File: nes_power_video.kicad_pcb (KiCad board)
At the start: 2 copper layers, 59.9 x 59.7 mm, 25 parts, among them J2 Audio, J3 Video, J4 Conn_01x05, J5 RGB conn feed, Q1 2SA733, U1 TPS2553DBV

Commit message: feat(power): add C4, a local 100nF bypass at the eFuse output
TI's TPS2553 layout guidelines (SLVSBM8, 12.1) ask for "a high-value
electrolytic capacitor and a 100-nF bypass capacitor on the output pin
when large transient currents are expected". /5V had neither locally.
C3 (100nF) bypasses the eFuse *input*; C1 (100uF) is the only thing on
the output and sits ~52mm of copper away, reached by a 20.5mm 0.2mm
spur that lands on D1's cathode pad. That routing is a fossil: C1
predates the eFuse (it was already placed when c00c4e2 inserted U1
into the middle of the rail), so the bulk cap ended up last in the
chain instead of at the source.

C4 is the same part as C3 (CC0805KRX7R9BB104, LCSC C49678) so this
adds a quantity, not a line, to the assembly BOM. Placed rotated 90
degrees at (32.3,35.5) so pad 1 lands directly on the /5V trace
leaving U1 pin 6 -- 3.56mm from the pin, against C1's 52mm -- with
pad 2 stitched to the B.Cu ground pour through its own via. The
rotation is what makes it fit: horizontal, the courtyard collided
with both R3 and R4. R6's reference text moved 2.6mm to clear C4's
pad 1.

This is an improvement, not a defect fix. Section 10.2.1.2.4 is
explicit that output capacitance "improves the performance of the
device" -- it is not a stability requirement, and the only stability
constraint in the datasheet (15k <= RILIM <= 232k) is already met by
R6 at 22k. Fabbed v2 boards are fine without it.

Verified: ERC 0 violations; DRC --schematic-parity --refill-zones
0 errors, 0 unconnected, 0 parity issues, and the warning count is
unchanged from before this commit (the same 6 pre-existing silkscreen
warnings on J2/J3); tools/check_nets.py passes with all 14 nets
identical between schematic and PCB.

Co-Authored-By: Claude Opus 5 <noreply@anthropic.com>
Claude-Session: https://claude.ai/code/session_01TQL5dscMjqktyVUuQL7XXJ
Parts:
- added C4: 100nF, Capacitor_SMD:C_0805_2012Metric_Pad1.18x1.45mm_HandSolder, F.Cu at (32.3, 35.5)
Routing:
- net GND: track 15.4 -> 16.9 mm, vias 7 -> 8
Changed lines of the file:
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@@
 		)
 	)
+	(footprint "Capacitor_SMD:C_0805_2012Metric_Pad1.18x1.45mm_HandSolder"
+		(layer "F.Cu")
+		(at 32.3 35.5 90)
+		(descr "Capacitor SMD 0805 (2012 Metric), square (rectangular) end terminal, IPC-7351 nominal with elongated pad for handsoldering. (Body size source: IPC-SM-782 page 76, https://www.pcb-3d.com/wordpress/wp-content/uploads/ipc-sm-782a_amendment_1_and_2.pdf, https://docs.google.com/spreadsheets/d/1BsfQQcO9C6DZCsRaXUlFlo91Tg2WpOkGARC1WS5S8t0/edit?usp=sharing)")
+		(tags "capacitor handsolder")
+		(property "Reference" "C4"
+			(at 4 0 90)
+			(layer "F.SilkS")
+			(effects
+				(font
+					(size 1 1)
+					(thickness 0.15)
+				)
+			)
+		)
+		(property "Value" "100nF"
+			(at 0 1.68 0)
+			(hide yes)
+			(layer "F.SilkS")
+			(effects
+				(font
+					(size 0.8 0.8)
+					(thickness 0.12)
+				)
+			)
+		)
+		(property "Datasheet" "https://www.lcsc.com/datasheet/C49678.pdf"
+			(at 0 0 0)
+			(layer "F.Fab")
+			(hide yes)
+			(effects
+				(font
+					(size 1.27 1.27)
+				)
+			)
+		)
+		(property "Description" "Unpolarized capacitor"
+			(at 0 0 0)
+			(layer "F.Fab")
+			(hide yes)
+			(effects
+				(font
+					(size 1.27 1.27)
+				)
+			)
+		)
+		(property "KiLib_Generator" "SMD_2terminal_chip_molded"
+			(at 0 0 0)
+			(layer "F.SilkS")
+			(hide yes)
+			(effects
+				(font
+					(size 1 1)
+					(thickness 0.15)
+				)
+			)
+		)
+		(property "Manufacturer" "YAGEO"
+			(at 0 0 0)
+			(layer "F.Fab")
+			(hide yes)
+			(effects
+				(font
+					(size 1.27 1.27)
+					(thickness 0.15)
+				)
+			)
+		)
+		(property "MPN" "CC0805KRX7R9BB104"
+			(at 0 0 0)
+			(layer "F.Fab")
+			(hide yes)
+			(effects
+				(font
+					(size 1.27 1.27)
+					(thickness 0.15)
+				)
+			)
+		)
+		(property "LCSC" "C49678"
+			(at 0 0 0)
+			(layer "F.Fab")
+			(hide yes)
+			(effects
+				(font
+					(size 1.27 1.27)
+					(thickness 0.15)
+				)
+			)
+		)
+		(property "Supplier Link" "https://www.lcsc.com/product-detail/C49678.html"
+			(at 0 0 0)
+			(layer "F.Fab")
+			(hide yes)
+			(effects
+				(font
+					(size 1.27 1.27)
+					(thickness 0.15)
+				)
+			)
+		)
+		(property "Spec" "100 nF +/-10%, 50 V, X7R, 0805 (any equivalent >=16 V X7R)"
+			(at 0 0 0)
+			(layer "F.Fab")
+			(hide yes)
+			(effects
+				(font
+					(size 1.27 1.27)
+					(thickness 0.15)
+				)
+			)
+		)
+		(attr smd)
+		(duplicate_pad_numbers_are_jumpers no)
+		(fp_line
+			(start -0.261252 -0.735)
+			(end 0.261252 -0.735)
+			(stroke
+				(width 0.12)
+				(type solid)
+			)
+			(layer "F.SilkS")
+		)
+		(fp_line
+			(start -0.261252 0.735)
+			(end 0.261252 0.735)
+			(stroke
+				(width 0.12)
+				(type solid)
+			)
+			(layer "F.SilkS")
+		)
+		(fp_rect
+			(start -1.88 -0.98)
+			(end 1.88 0.98)
+			(stroke
+				(width 0.05)
+				(type solid)
+			)
+			(fill no)
+			(layer "F.CrtYd")
+		)
+		(fp_rect
+			(start -1 -0.625)
+			(end 1 0.625)
+			(stroke
+				(width 0.1)
+				(type solid)
+			)
+			(fill no)
+			(layer "F.Fab")
+		)
+		(fp_text user "${REFERENCE}"
+			(at 0 0 0)
+			(layer "F.Fab")
+			(effects
+				(font
+					(size 0.5 0.5)
+					(thickness 0.08)
+				)
+			)
+		)
+		(pad "1" smd roundrect
+			(at -1.0375 0 90)
+			(size 1.175 1.45)
+			(layers "F.Cu" "F.Mask" "F.Paste")
+			(roundrect_rratio 0.212766)
+			(net "/5V")
+		)
+		(pad "2" smd roundrect
+			(at 1.0375 0 90)
+			(size 1.175 1.45)
+			(layers "F.Cu" "F.Mask" "F.Paste")
+			(roundrect_rratio 0.212766)
+			(net "GND")
+		)
+		(embedded_fonts no)
+		(model "${KICAD10_3DMODEL_DIR}/Capacitor_SMD.3dshapes/C_0805_2012Metric.step"
+			(offset
+				(xyz 0 0 0)
+			)
+			(scale
+				(xyz 1 1 1)
+			)
+			(rotate
+				(xyz 0 0 0)
+			)
+		)
+	)
 	(footprint "nes1:PJRAN1X1U03X"
 		(layer "F.Cu")
@@
 		(tags "resistor handsolder")
 		(property "Reference" "R6"
-			(at 0 -1.65 0)
+			(at 2.6 -1.65 0)
 			(layer "F.SilkS")
 			(effects
@@
 		(net "Net-(Q1-B)")
 	)
+	(segment
+		(start 32.3 34.4625)
+		(end 32.3 33.0)
+		(width 0.4)
+		(layer "F.Cu")
+		(net "GND")
+	)
+	(via
+		(at 32.3 33.0)
+		(size 0.6)
+		(drill 0.3)
+		(layers "F.Cu" "B.Cu")
+		(net "GND")
+	)
 	(zone

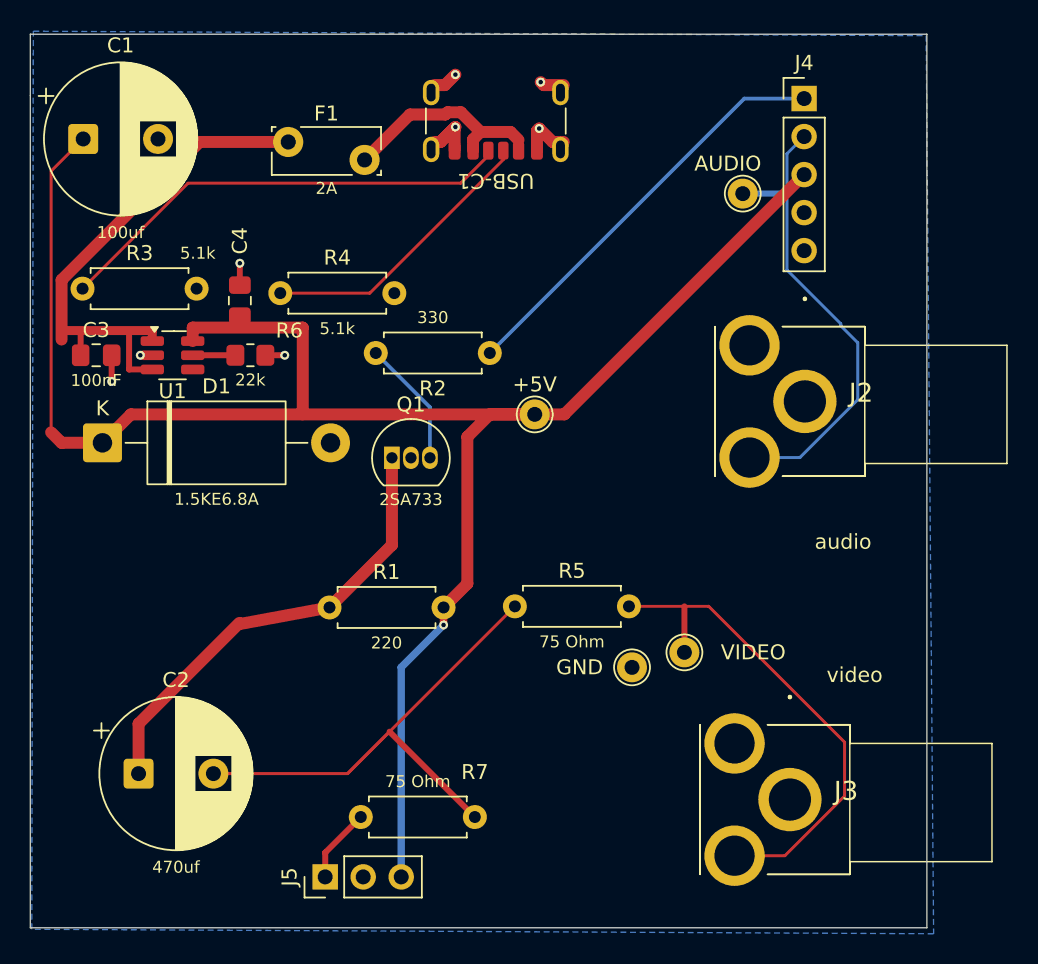
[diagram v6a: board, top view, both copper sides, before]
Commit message: fix(pcb): remove every overlapping track, and anchor C4's /5V connection
A geometric sweep for collinear same-net overlap found five pairs, not
the one spotted by eye in 2987996. Same-net overlap is invisible to
DRC, so none of these were ever reported.

  /5V         3.00mm  b7a635ae sat entirely inside the y=43.1 trunk
  /VIDEO_BUF  3.96mm  0d07e40b sat entirely inside a94ae6b3
  GND         1.27mm  4d3f7556 spanned what 387e46eb + 67cc2dcf already
  GND         0.14mm  the tail of that same knot
  /fused_5v   0.60mm  da31efaa doubled back over 1f43262f

The GND knot is resolved by deleting the single full-span segment
rather than the two-piece chain: 56acf260 lands on the intermediate
point (46.6,24.0), so keeping the chain preserves endpoint-to-endpoint
connectivity instead of relying on a T-junction.

/fused_5v needed a trim, not just a delete. 1f43262f overshot the
junction at (20.39,37.5) down to 38.1 and da31efaa doubled back up, so
removing the stub alone would have left a 0.6mm dangling tail. Its end
is now the junction itself.

Also anchors C4. Its pad 1 was touching the /5V trace only through a
1.45 x 0.225mm area overlap -- enough for KiCad to call it connected,
but far too little to rely on. An explicit 0.76mm stub from the pad
centre to the trace centreline now carries it.

Copper removed, per net, matching prediction exactly and touching
nothing else: /5V -3.000mm, /VIDEO_BUF -3.960mm, /fused_5v -1.200mm,
GND -1.414mm. Ten other nets unchanged to the picometre.

Verified: geometric overlap sweep 0 pairs across 92 segments; DRC
--schematic-parity --refill-zones 0 errors, 0 unconnected, 0 parity,
warnings unchanged at the 6 pre-existing J2/J3 silkscreen ones;
check_nets.py all invariants, 14/14 nets identical; and an independent
union-find over pads, tracks and vias confirms all 13 non-GND nets are
a single copper island each, with 0 of 63 pads outside the board
outline, 0 pads lacking track contact and 0 dangling endpoints.

Co-Authored-By: Claude Opu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
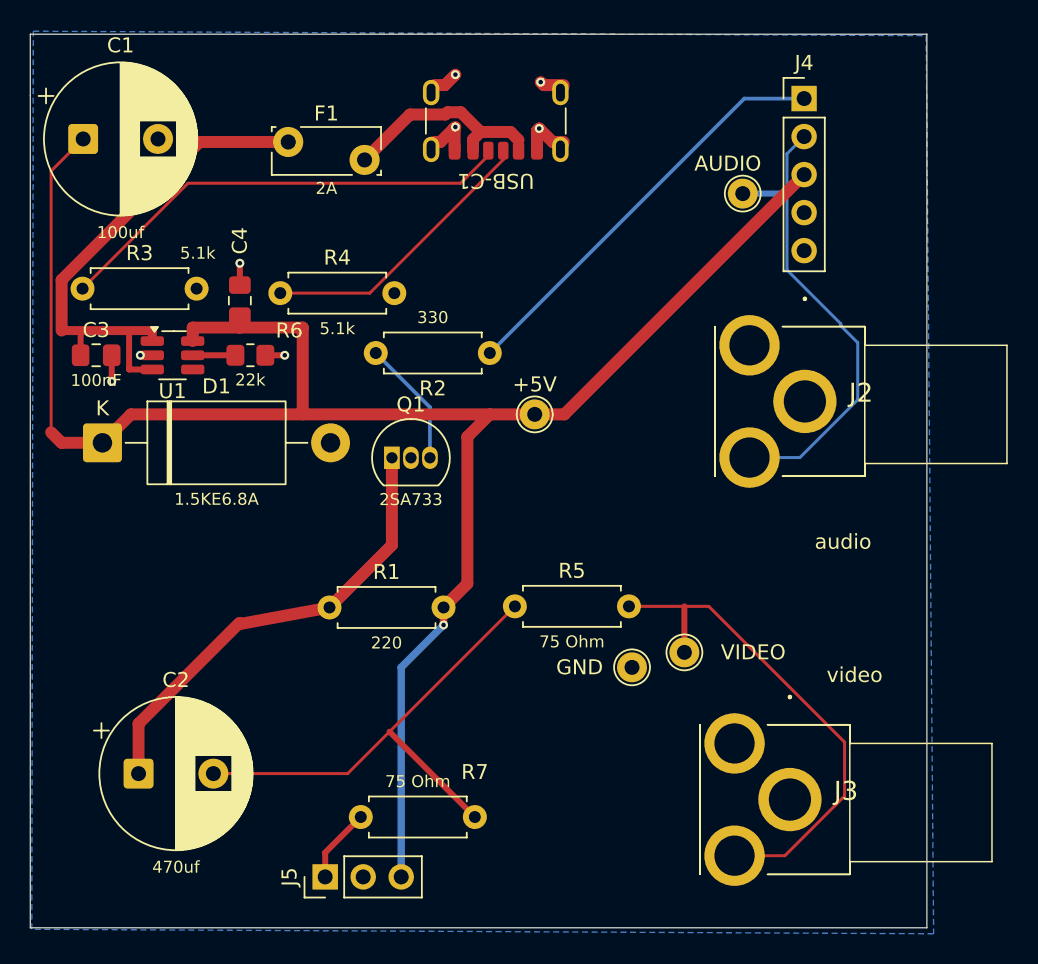
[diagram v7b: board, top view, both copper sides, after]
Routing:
- net /VIDEO_BUF: track 36.8 -> 32.8 mm
- net /5V: track 128.9 -> 126.7 mm
- net GND: track 16.9 -> 15.5 mm
- net /fused_5v: track 36.1 -> 34.9 mm
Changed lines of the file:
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@@
-	)
-	(segment
-		(start 49 43.1)
-		(end 52 43.1)
-		(width 0.8)
-		(layer "F.Cu")
-		(net "/5V")
 	)
 	(segment
@@
 	)
 	(segment
-		(start 45.7 24.9)
-		(end 46.7 23.9)
-		(width 0.8)
-		(layer "F.Cu")
-		(net "GND")
-	)
-	(segment
 		(start 46.65 24.05)
 		(end 46.6 24)
@@
 	(segment
 		(start 20.39 34.1201)
-		(end 20.39 38.1)
+		(end 20.39 37.5)
 		(width 0.8)
 		(layer "F.Cu")
@@
 	)
 	(segment
-		(start 20.39 38.1)
-		(end 20.39 37.5)
-		(width 0.6)
-		(layer "F.Cu")
-		(net "/fused_5v")
-	)
-	(segment
 		(start 47.88 25.5649)
 		(end 47.88 25.48)
@@
 		(layer "F.Cu")
 		(net "Net-(Q1-E)")
-	)
-	(segment
-		(start 39.5 67.1)
-		(end 42.3 64.3)
-		(width 0.2)
-		(layer "F.Cu")
-		(net "/VIDEO_BUF")
 	)
 	(segment
@@
 		(net "GND")
 	)
+	(segment
+		(start 32.3 36.5375)
+		(end 32.3 37.3)
+		(width 0.8)
+		(layer "F.Cu")
+		(net "/5V")
+	)
 	(zone
